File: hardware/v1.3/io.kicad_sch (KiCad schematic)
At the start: 3 parts, among them J6 Micro_SD_Card_Det2, U1 ECP5-CABGA256

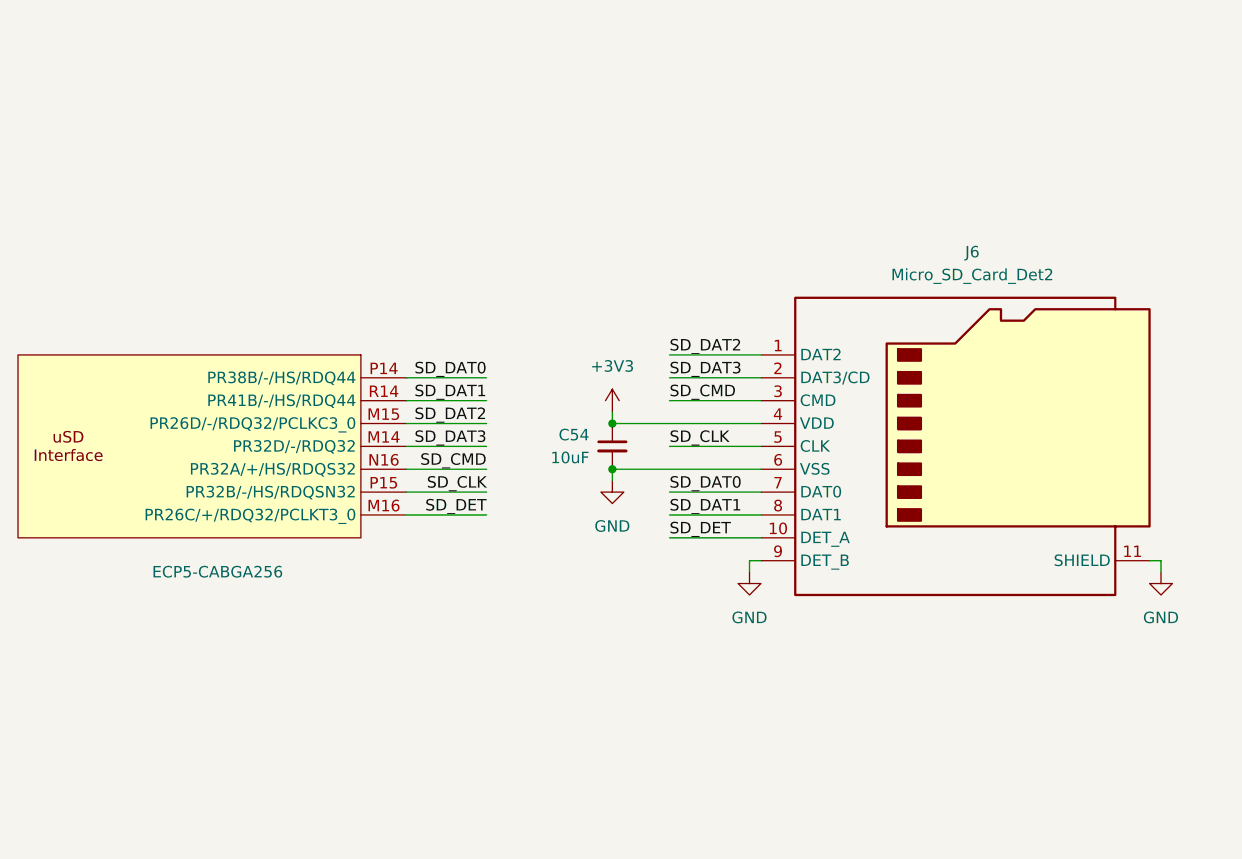
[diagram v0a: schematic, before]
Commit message: Improve makefile and hardware
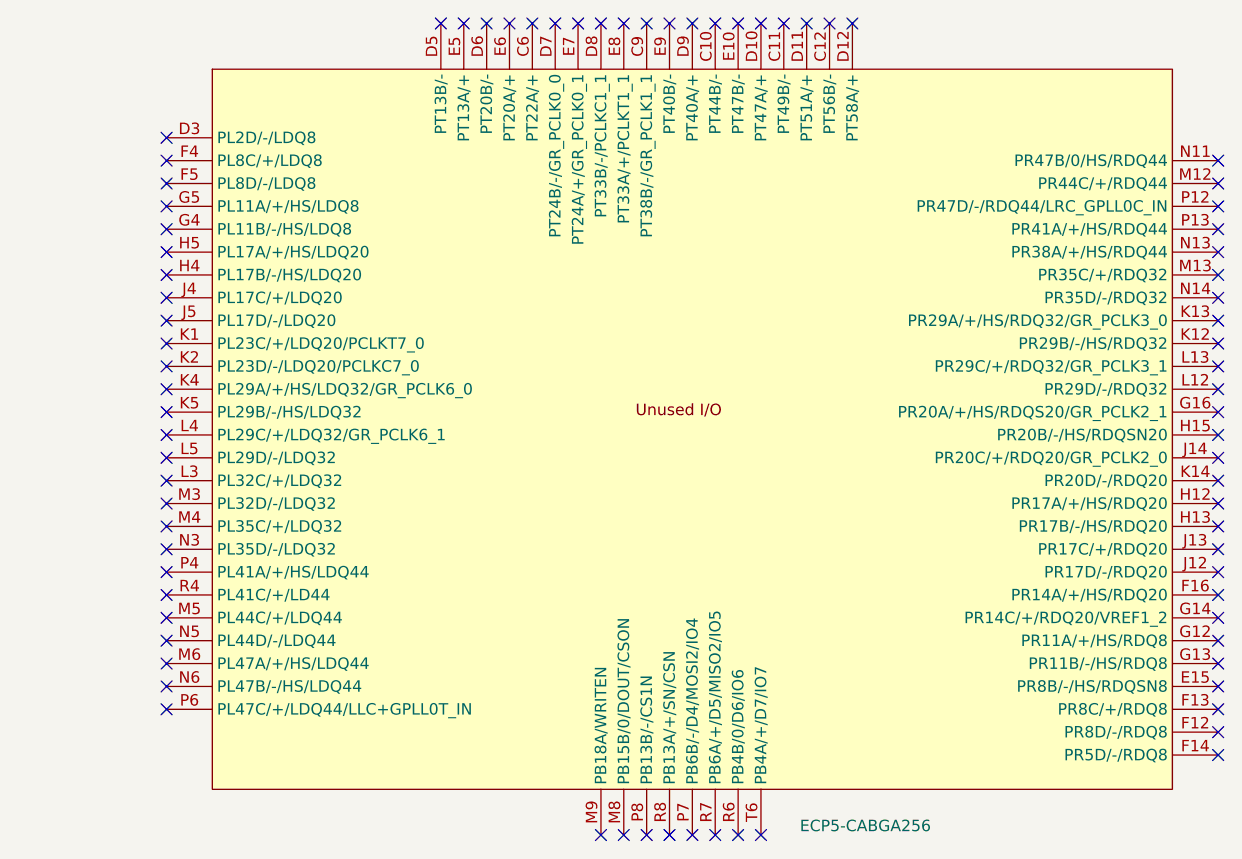
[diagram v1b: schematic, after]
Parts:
- removed C54: 10uF, Capacitor_SMD:C_0603_1608Metric, symbol Device:C_Small
- removed J6: Micro_SD_Card_Det2, icepi-lib:microSD_HC_SOFNG_TF-008, symbol Connector:Micro_SD_Card_Det2
- removed U1: ECP5-CABGA256, Package_BGA:BGA-256_14.0x14.0mm_Layout16x16_P0.8mm_Ball0.45mm_Pad0.32mm_NSMD, symbol icepi-lib:LFE5U-25F-6BG256x
- added U1: ECP5-CABGA256, Package_BGA:BGA-256_14.0x14.0mm_Layout16x16_P0.8mm_Ball0.45mm_Pad0.32mm_NSMD, symbol icepi-lib:LFE5U-25F-6BG256x
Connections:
- no-connect marks 0 -> 80
